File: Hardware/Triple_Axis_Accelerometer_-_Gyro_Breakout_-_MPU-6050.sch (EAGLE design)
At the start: 17 parts, among them U1 MPU-6050-1, U3 CREATIVE_COMMONS

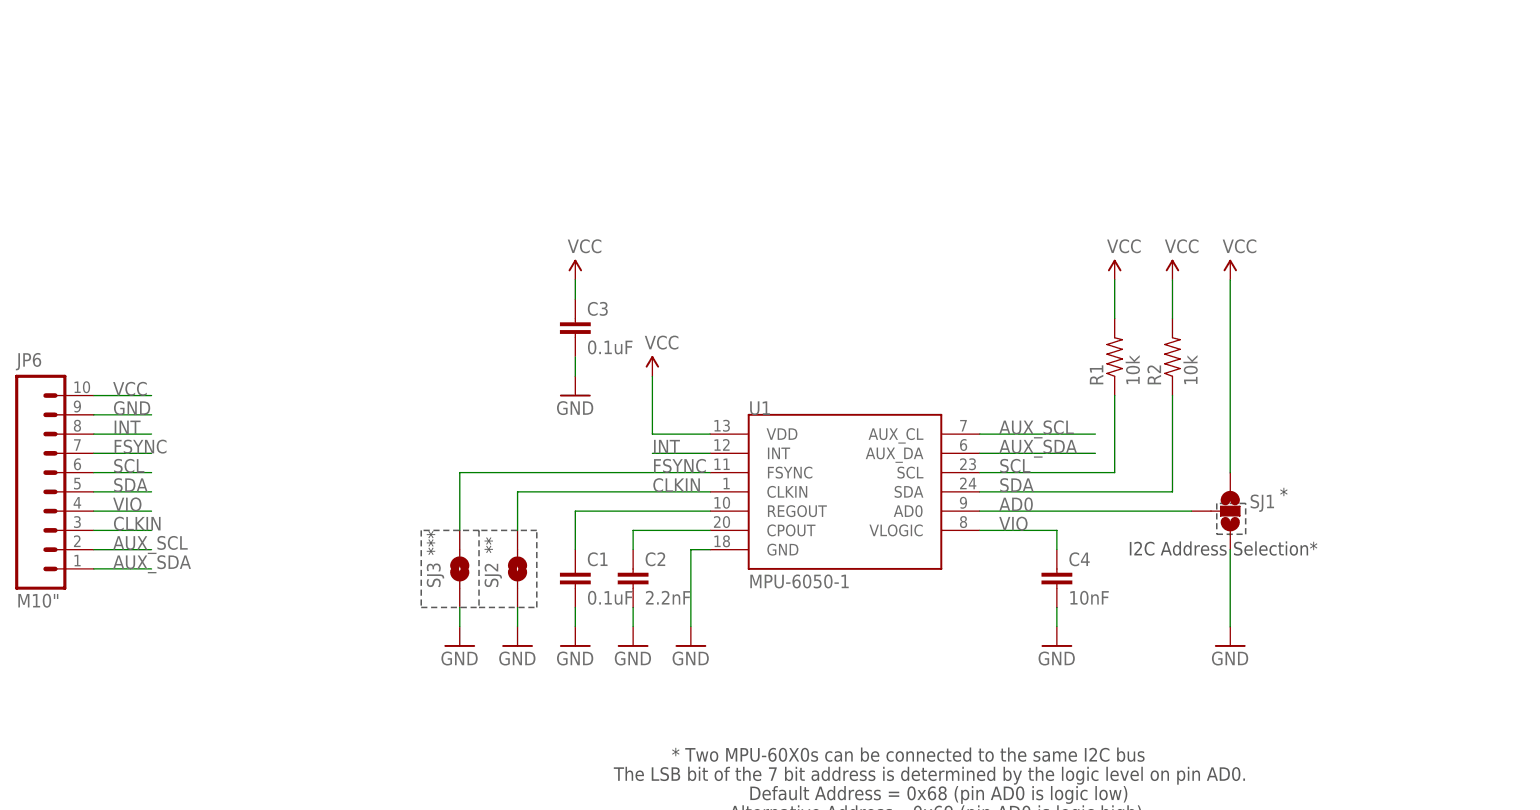
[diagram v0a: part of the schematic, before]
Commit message: Package 0402 >>0603, cleaned up schematic, gitignore
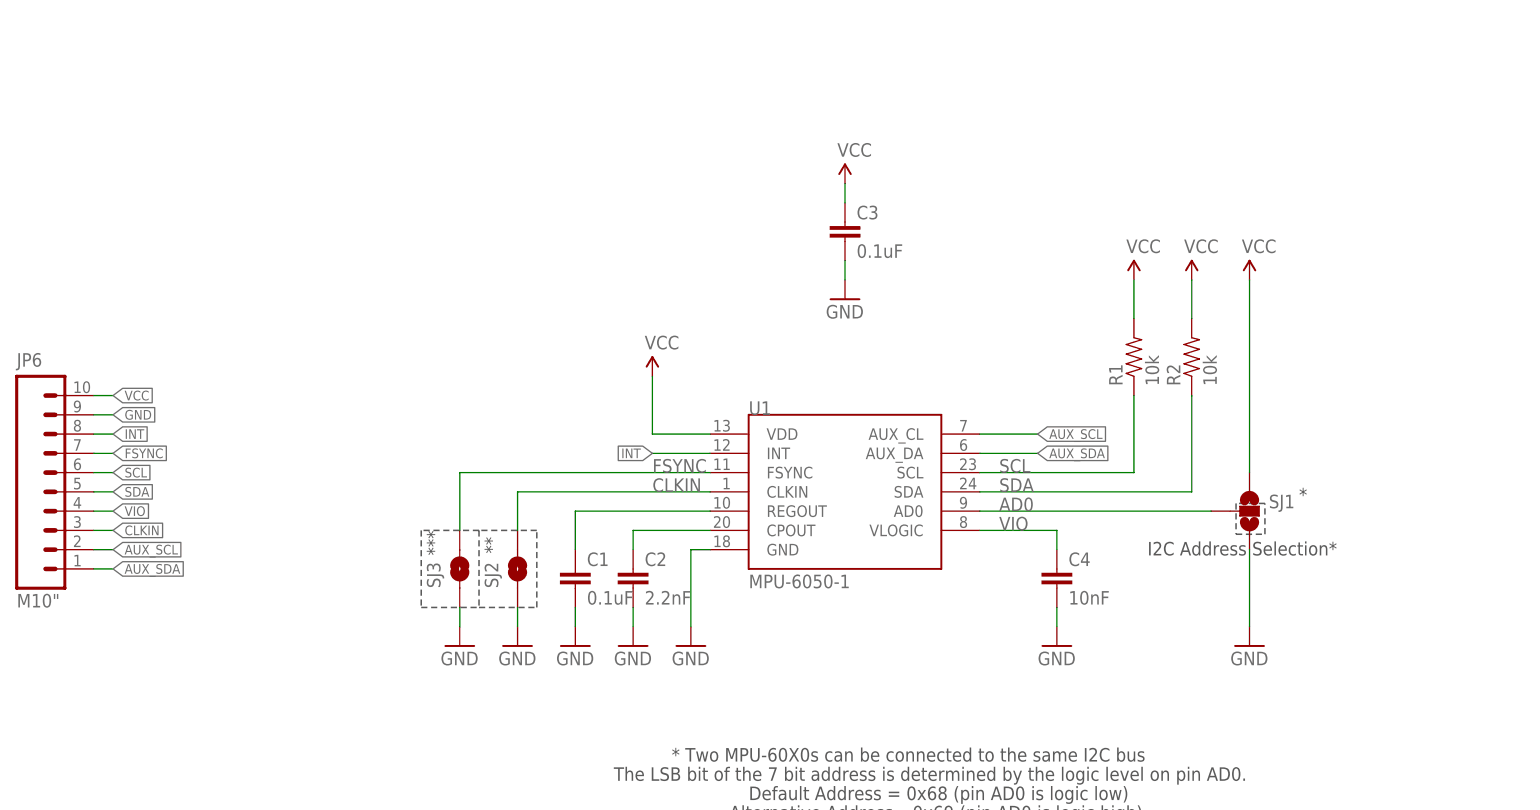
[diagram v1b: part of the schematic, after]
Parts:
- C1, C2, C3, C4: device SparkFun:CAP0402-CAP -> SparkFun:CAP0603-CAP
- R1, R2: device SparkFun:RESISTOR0402-RES -> SparkFun:RESISTOR0603-RES
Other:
- moved on the sheet: C3, R1, R2, SJ1

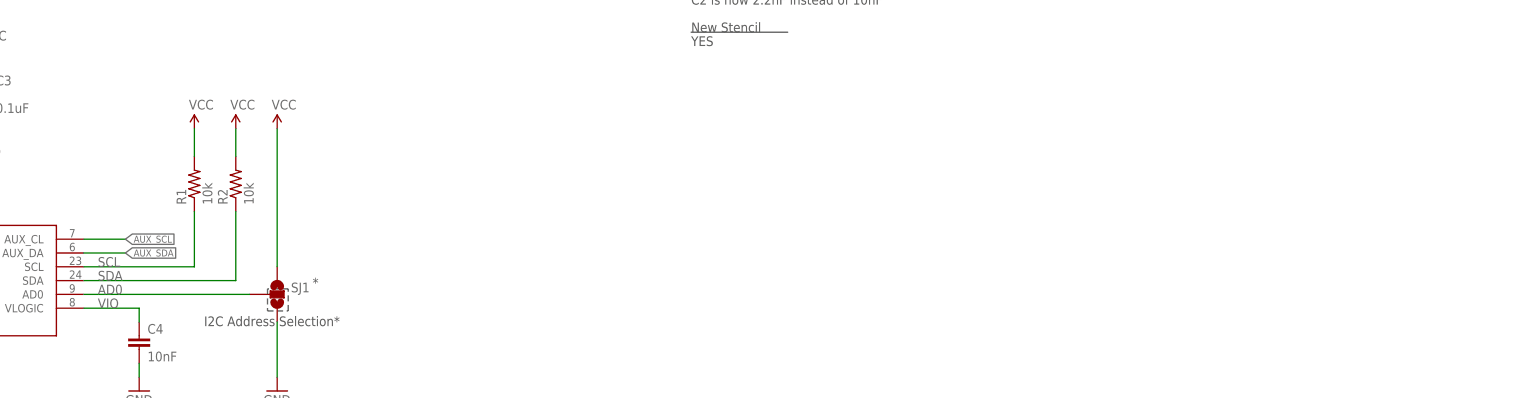
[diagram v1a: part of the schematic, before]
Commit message: Cleaned up silk and schematic
-Moved via so that it is not under the "sync" or the "AD0" silk
-Changed Z-axis silk to circle w/ dot (from circle with X)
-added changes (code) on schematic
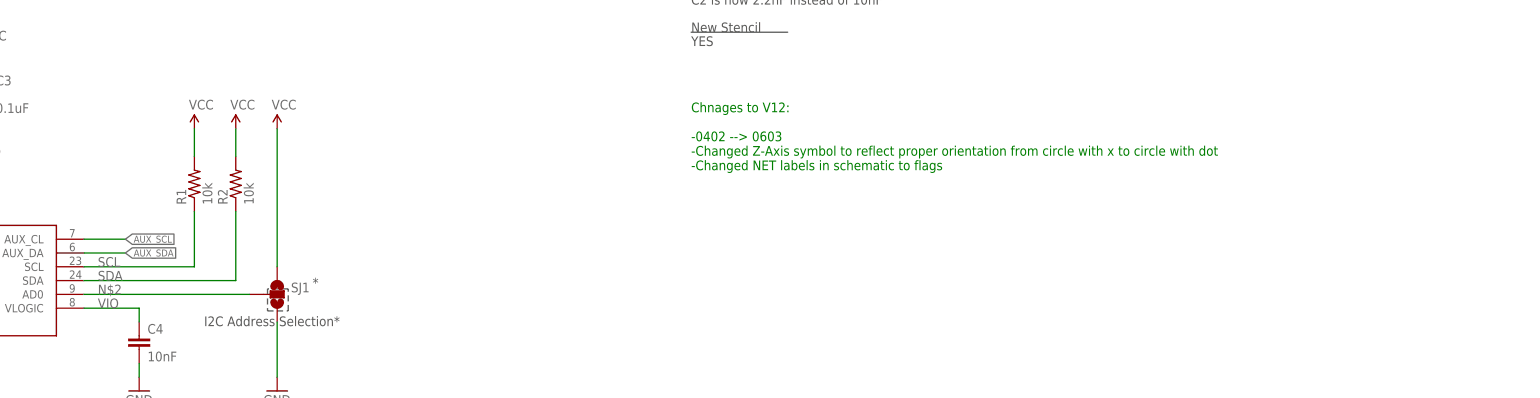
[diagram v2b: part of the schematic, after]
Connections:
- net AD0 renamed N$2
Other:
- note added: "Chnages to V12: -0402 --> 0603 -Changed Z-Axis symbol to reflect proper orientation from circle with x to circle with dot -Changed NET labels in schematic to flags"
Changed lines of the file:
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@@
 <wire x1="173.482" y1="105.156" x2="173.482" y2="101.092" width="0.2032" layer="97" style="shortdash"/>
 <text x="251.46" y="167.64" size="1.778" layer="97">Played around with IC footprint. Added 4 small tcream squares to middle pad. Rounded and elongated pads.</text>
+<text x="251.46" y="127" size="1.778" layer="91">Chnages to V12:
+-0402 --&gt; 0603
+-Changed Z-Axis symbol to reflect proper orientation from circle with x to circle with dot
+-Changed NET labels in schematic to flags</text>
 </plain>
 <instances>
@@
 </segment>
 </net>
-<net name="AD0" class="0">
+<net name="N$2" class="0">
 <segment>
 <label x="142.24" y="104.14" size="1.778" layer="95"/>
@@
 </schematic>
 </drawing>
+<compatibility>
+<note version="6.3" minversion="6.2.2" severity="warning">
+Since Version 6.2.2 text objects can contain more than one line,
+which will not be processed correctly with this version.
+</note>
+</compatibility>
 </eagle>

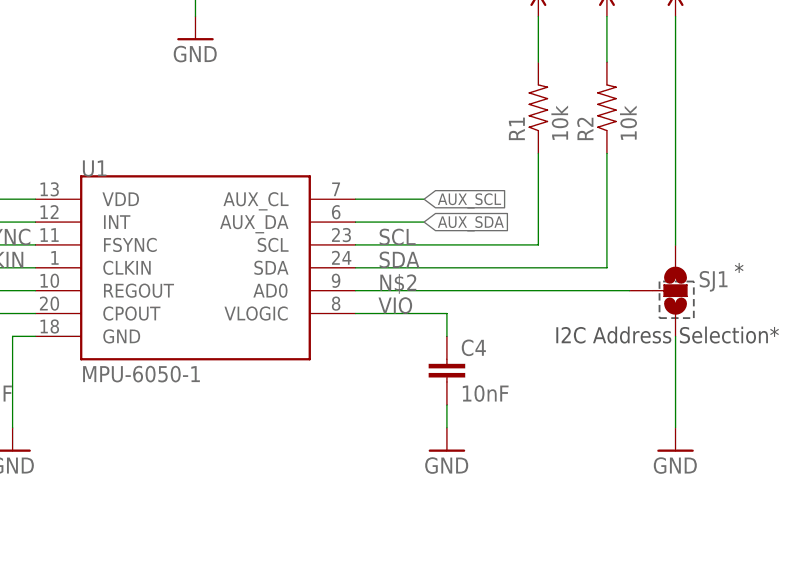
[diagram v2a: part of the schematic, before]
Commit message: Fixed Air-wire on ADO line
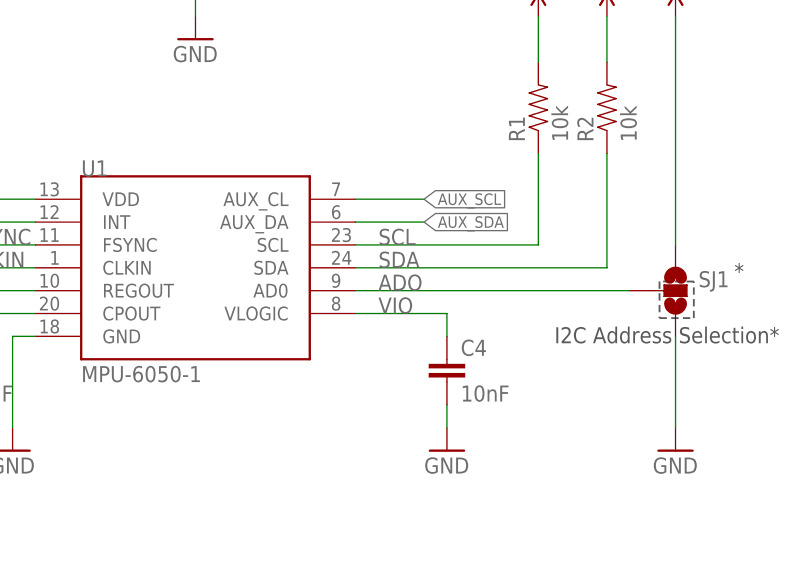
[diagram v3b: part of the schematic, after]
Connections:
- net N$2 renamed ADO
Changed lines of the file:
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@@
 </segment>
 </net>
-<net name="N$2" class="0">
+<net name="ADO" class="0">
 <segment>
 <label x="142.24" y="104.14" size="1.778" layer="95"/>

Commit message: Fixed formatting issues on schematic and board file
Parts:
- removed U3: CREATIVE_COMMONS, SparkFun:CREATIVE_COMMONS
- added FRAME1: FRAME-LETTER, SparkFun-Aesthetics:FRAME-LETTER
- added U$5: REVISION, SparkFun-Aesthetics:REVISION
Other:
- note added: "Added 4 small tcream squares to middle pad."
- note added: "C2 was mislabled as 10nF, should have been 2.2nF."
- note added: "Changes to V12: -0402 --> 0603 -Changed Z-Axis symbol to reflect proper orientation from circle with x to circle with dot -Changed NET labels in schematic to flags"
- note added: "E. Orosel"
- note added: "J. Bartlett"
- note added: "Played around with IC footprint."
- note added: "Rounded and elongated pads."
- note added: "v12"
- note removed: "C2 was mislabled as 10nF, should have been 2.2nF. Fixed in V11"
- note removed: "Chnages to V12: -0402 --> 0603 -Changed Z-Axis symbol to reflect proper orientation from circle with x to circle with dot -Changed NET labels in schematic to flags"
- note removed: "Joel Bartlett"
- note removed: "Played around with IC footprint. Added 4 small tcream squares to middle pad. Rounded and elongated pads."
- moved on the sheet: C1, C2, C3, C4, JP6, R1, R2, SJ1, SJ2, SJ3, U1
